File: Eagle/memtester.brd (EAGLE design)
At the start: 80.1 x 23.2 mm, 4 parts

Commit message: Memtester: part work backup
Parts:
- added U$2, U$3: PCF8575TS, PCF8575TS:SSOP24
- U$1: value NN5118160AJ -> NN5118160AJSOCKET; device AtariST:SOJ127P1117X376-42 -> memory:SOJ42SOCKET
- moved C3 28.4 mm to (9.91, 1.46), flipped to the bottom
- moved C2 11.4 mm to (33.1, 5.96), flipped to the bottom
- moved C1 11.4 mm to (1.99, 5.90), flipped to the bottom
- moved U$1 6.85 mm to (17.5, 12.1), turned to 0 degrees
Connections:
- new net A0: U$1.17, U$3.4
- new net A1: U$1.18, U$3.5
- new net A2: U$1.19, U$3.6
- new net A3: U$1.20, U$3.7
- new net A4: U$1.23, U$3.8
- new net A5: U$1.24, U$3.9
- new net A6: U$1.25, U$3.10
- new net A7: U$1.26, U$3.11
- new net A8: U$1.27, U$3.13
- new net A9: U$1.28, U$3.14
- new net D0: U$1.2, U$2.4
- new net D1: U$1.3, U$2.5
- new net D10: U$1.35, U$2.15
- new net D11: U$1.36, U$2.16
- new net D12: U$1.38, U$2.17
- new net D13: U$1.39, U$2.18
- new net D14: U$1.40, U$2.19
- new net D15: U$1.41, U$2.20
- new net D2: U$1.4, U$2.6
- new net D3: U$1.5, U$2.7
- new net D4: U$1.7, U$2.8
- new net D5: U$1.8, U$2.9
- new net D6: U$1.9, U$2.10
- new net D7: U$1.10, U$2.11
- new net D8: U$1.33, U$2.13
- new net D9: U$1.34, U$2.14
- new net I2C_SCL: U$2.22, U$3.22
- new net I2C_SDA: U$2.23, U$3.23
- net +5V: now also U$2.21, U$2.24, U$2.3, U$3.24, U$3.3
- net GND: now also U$2.12, U$2.2, U$3.12, U$3.2, U$3.21
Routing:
- net D0: track 0.00 -> 43.7 mm
- net D14: track 0.00 -> 39.7 mm
- net D2: track 0.00 -> 39.7 mm
- net D15: track 0.00 -> 39.2 mm
- net D1: track 0.00 -> 39.0 mm
- net A0: track 0.00 -> 37.8 mm
- net A9: track 0.00 -> 37.0 mm, vias 0 -> 1
- net D12: track 0.00 -> 36.1 mm
- net D13: track 0.00 -> 35.4 mm
- net D3: track 0.00 -> 35.3 mm
- net A7: track 0.00 -> 35.0 mm, vias 0 -> 1
- net A2: track 0.00 -> 34.0 mm
- net A5: track 0.00 -> 33.8 mm, vias 0 -> 1
- net A1: track 0.00 -> 33.5 mm
- net D11: track 0.00 -> 32.9 mm
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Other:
- board size 80.1 x 23.2 mm -> 69 x 22.6 mm
- board text added: "MEMTester"
- board text removed: "STRam Rev.C"

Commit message: Memtester: part work
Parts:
- added C4: 100nF, resistor:C0402
- added C5, C6: 100nF, passives:0402_CAP
- added IC1: HT7833, holtek2:SOT-89
- added J3: SM08B-SRSS-TB(LF)(SN), SM08B-SRSS-TB_LF__SN_:JST_SM08B-SRSS-TB(LF)(SN)
- added PROG: (no value), pinhead:1X03
- added U$6: OLED_0.96_I2CNO_DRILL, tft_1_8_1_44_oled_0_96:OLED_0.96_I2C_NO_DRILL
- added U1: ATTINY1616-MFR, ATTINY1616-MFR:QFN40P300X300X90-21N
- added UART: (no value), pinhead:1X04
- C1, C2, C3: device rcl:C0805 -> passives:0402_CAP
- moved U$3 2.25 mm to (49.8, 12.1)
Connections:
- new net EXTCLK: U1.2
- new net N$1: IC1.1, U$6.VCC
- new net OE: U$1.29, U$3.17
- new net PA5: U1.6
- new net PA6: U1.7
- new net PA7: U1.8
- new net PB2: U1.12
- new net PB3: U1.11
- new net PB4: U1.10
- new net PB5: U1.9
- new net RTS: U1.5
- new net RXD: U1.1, UART.2
- new net SPI_CS: J3.5, U1.18
- new net SPI_MISO: J3.6, U1.16
- new net SPI_MOSI: J3.3, U1.17
- new net SPI_SCLK: J3.4, U1.15
- new net TINY_RST: PROG.1, U1.19
- new net TXD: U1.20, UART.1
- net +5V: now also C4.1, C5.1, C6.1, IC1.3, IC1.4, J3.2, PROG.2, U1.4, UART.3
- net CAS0H: now also U$3.16
- net CAS0L: now also U$3.15
- net GND: now also C4.2, C5.2, C6.2, IC1.2, J3.1, PROG.3, U$6.GND, U1.21, U1.3, UART.4; no longer U$1.29
- net I2C_SCL: now also J3.7, U$6.SCL, U1.14
- net I2C_SDA: now also J3.8, U$6.SDA, U1.13
- net WE: now also U$3.18
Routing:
- net +5V: track 10.2 -> 147.9 mm, vias 0 -> 6
- net WE: track 0.00 -> 39.0 mm, vias 0 -> 1
- net CAS0L: track 0.00 -> 37.1 mm, vias 0 -> 1
- net I2C_SCL: track 0.00 -> 36.4 mm, vias 0 -> 2
- net OE: track 0.00 -> 35.2 mm, vias 0 -> 1
- net I2C_SDA: track 0.00 -> 33.4 mm, vias 0 -> 2
- net CAS0H: track 0.00 -> 33.1 mm, vias 0 -> 1
- net N$1: track 0.00 -> 14.3 mm
- net SPI_CS: track 0.00 -> 13.1 mm, vias 0 -> 2
- net TINY_RST: track 0.00 -> 12.8 mm
- net SPI_MOSI: track 0.00 -> 12.7 mm, vias 0 -> 2
- net SPI_MISO: track 0.00 -> 11.4 mm, vias 0 -> 2
- net SPI_SCLK: track 0.00 -> 10.8 mm, vias 0 -> 2
- net TXD: track 0.00 -> 9.25 mm, vias 0 -> 1
- net RXD: track 0.00 -> 8.25 mm, vias 0 -> 1
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- added copper zone on layer 1, net GND
- removed copper zone on layer 1, net +5V
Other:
- board size 69 x 22.6 mm -> 69 x 22.3 mm
- board text added: "5V"
- board text added: "CS"
- board text added: "GND"
- board text added: "MISO"
- board text added: "MOSI"
- board text added: "RST"
- board text added: "RX0"
- board text added: "SCL"
- board text added: "SCLK"
- board text added: "SDA"
- board text added: "TX0"

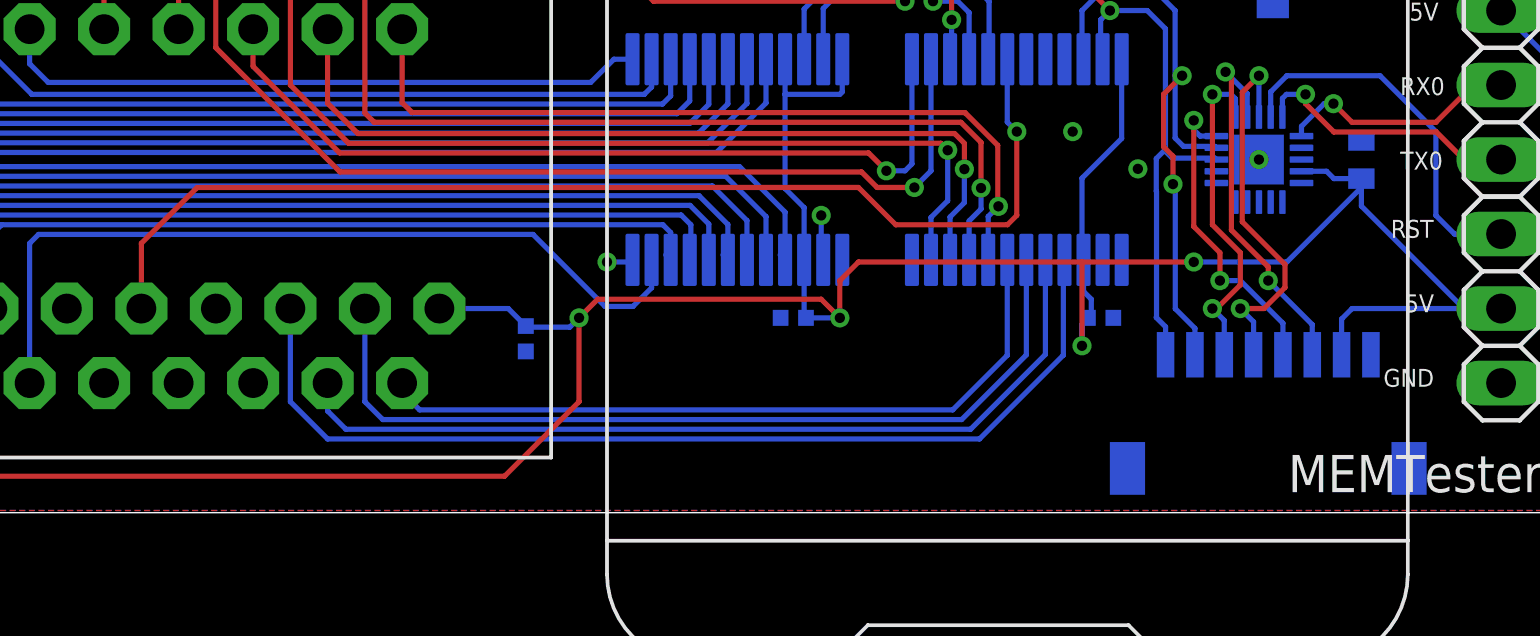
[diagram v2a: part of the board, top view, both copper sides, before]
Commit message: Memtester: routed RAS0
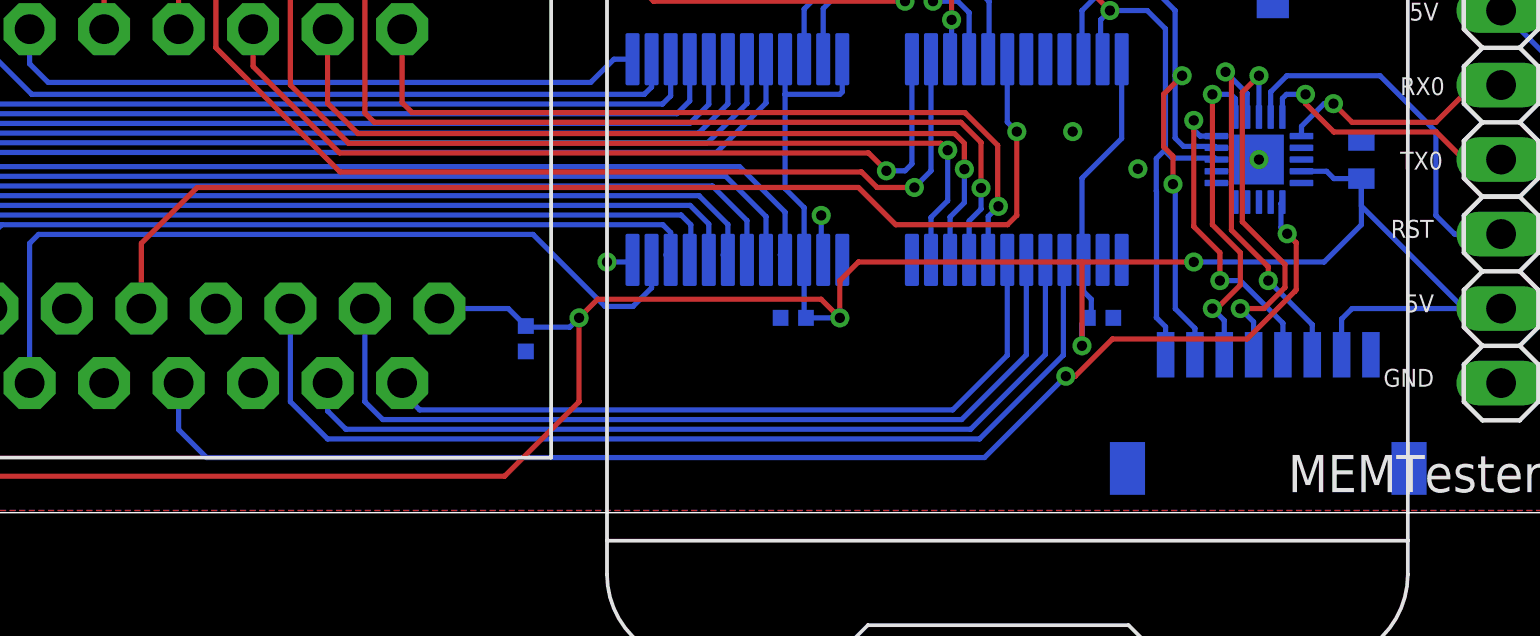
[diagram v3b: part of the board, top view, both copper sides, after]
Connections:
- removed net PA5: U1.6
- net RAS0: now also U1.6
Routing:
- net RAS0: track 0.00 -> 45.7 mm, vias 0 -> 2
- net +5V: track 147.9 -> 148.6 mm
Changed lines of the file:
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@@
 <wire x1="52.07" y1="6.46556875" x2="52.07" y2="5.715" width="0.1778" layer="16"/>
 <via x="52.07" y="5.715" extent="1-16" drill="0.35"/>
-<wire x1="61.595" y1="11.415" x2="61.595" y2="11.1125" width="0.1778" layer="16"/>
-<wire x1="61.595" y1="11.1125" x2="59.055" y2="8.5725" width="0.1778" layer="16"/>
-<wire x1="59.055" y1="8.5725" x2="55.88" y2="8.5725" width="0.1778" layer="16"/>
+<wire x1="61.595" y1="11.415" x2="61.595" y2="9.8425" width="0.1778" layer="16"/>
+<wire x1="61.595" y1="9.8425" x2="60.325" y2="8.5725" width="0.1778" layer="16"/>
+<wire x1="60.325" y1="8.5725" x2="55.88" y2="8.5725" width="0.1778" layer="16"/>
 <contactref element="UART" pad="3"/>
 <wire x1="61.92750625" y1="11.415" x2="61.595" y2="11.415" width="0.1778" layer="16"/>
@@
 <signal name="RAS0">
 <contactref element="U$1" pad="14"/>
+<contactref element="U1" pad="6"/>
+<wire x1="22.225" y1="1.905" x2="21.2725" y2="2.8575" width="0.1778" layer="16"/>
+<wire x1="21.2725" y1="4.445" x2="21.2725" y2="2.8575" width="0.1778" layer="16"/>
+<wire x1="48.74676875" y1="1.905" x2="51.519634375" y2="4.677865625" width="0.1778" layer="16"/>
+<via x="51.519634375" y="4.677865625" extent="1-16" drill="0.35"/>
+<wire x1="59.3189" y1="7.56515625" x2="59.3189" y2="7.5664" width="0.1778" layer="1"/>
+<wire x1="59.3189" y1="7.5664" x2="59.3725" y2="7.62" width="0.1778" layer="1"/>
+<wire x1="53.107134375" y1="5.947865625" x2="51.837134375" y2="4.677865625" width="0.1778" layer="1"/>
+<wire x1="51.519634375" y1="4.677865625" x2="51.837134375" y2="4.677865625" width="0.1778" layer="1"/>
+<wire x1="57.701609375" y1="5.947865625" x2="53.107134375" y2="5.947865625" width="0.1778" layer="1"/>
+<wire x1="57.701609375" y1="5.947865625" x2="59.3189" y2="7.56515625" width="0.1778" layer="1"/>
+<wire x1="59.3725" y1="7.62" x2="59.3725" y2="9.2285375" width="0.1778" layer="1"/>
+<wire x1="59.3725" y1="9.2285375" x2="59.06551875" y2="9.53551875" width="0.1778" layer="1"/>
+<via x="59.06551875" y="9.53551875" extent="1-16" drill="0.35"/>
+<wire x1="59.06551875" y1="9.53551875" x2="58.8538" y2="9.7472375" width="0.1778" layer="16"/>
+<wire x1="58.8538" y1="10.5663" x2="58.8538" y2="9.7472375" width="0.1778" layer="16"/>
+<wire x1="58.8538" y1="10.5663" x2="58.9025" y2="10.615" width="0.1778" layer="16"/>
+<wire x1="22.225" y1="1.905" x2="48.74676875" y2="1.905" width="0.1778" layer="16"/>
 </signal>
 <signal name="CAS0H">
@@
 <contactref element="U1" pad="2"/>
 </signal>
-<signal name="PA5">
-<contactref element="U1" pad="6"/>
-</signal>
 <signal name="PA6">

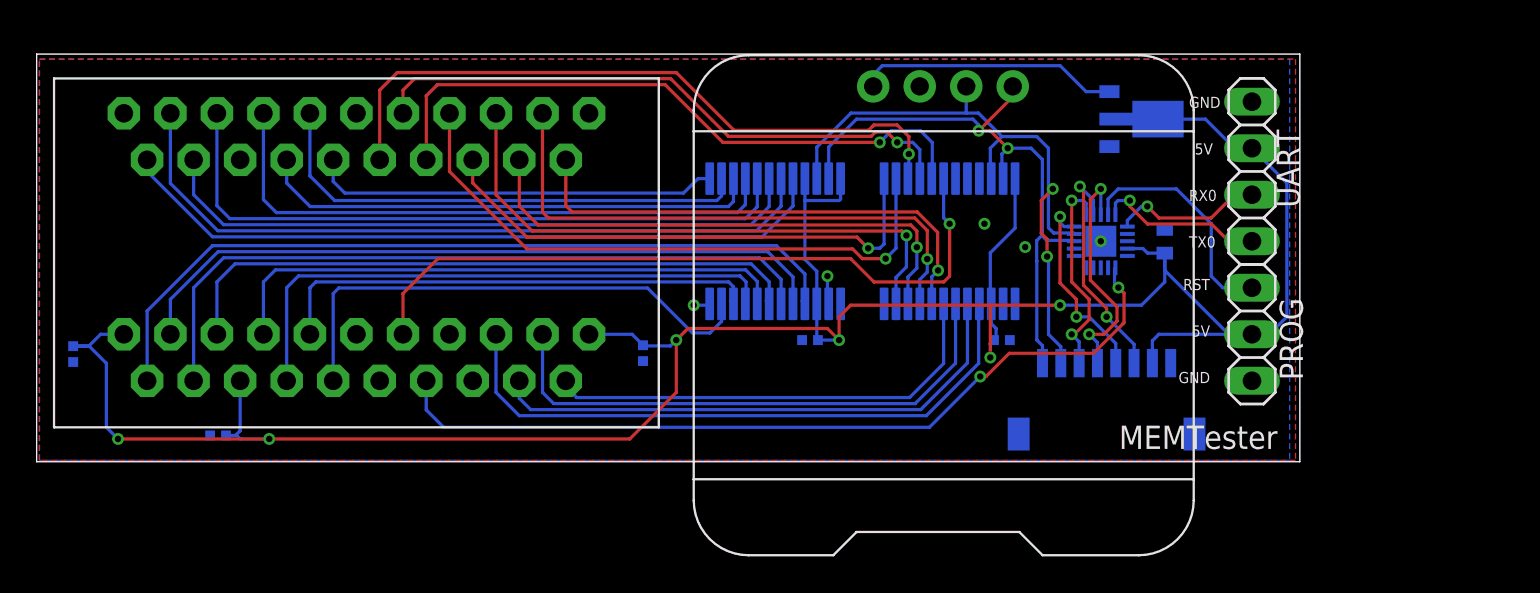
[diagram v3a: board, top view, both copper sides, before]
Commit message: Memtester: bigger 5v wire
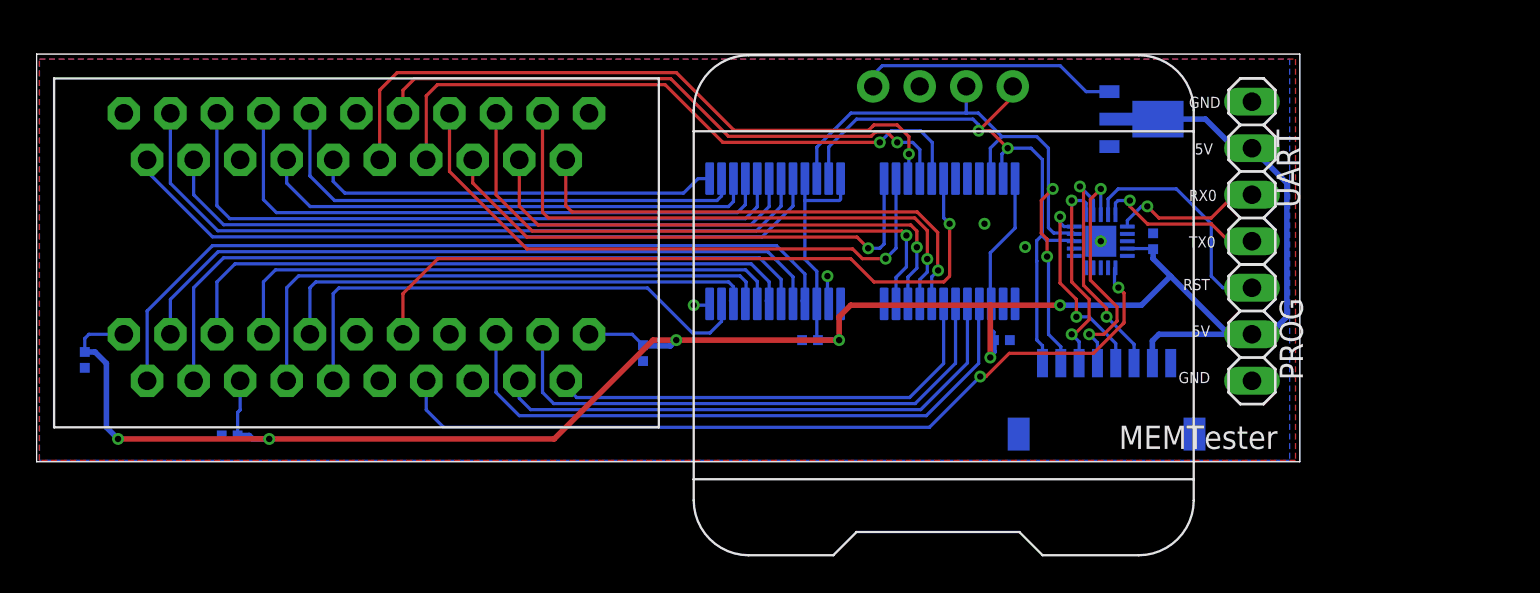
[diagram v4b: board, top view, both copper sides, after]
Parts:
- C4: device resistor:C0402 -> passives:0402_CAP
- moved C1 0.71 mm to (2.63, 5.59)
- moved C3 0.63 mm to (10.5, 1.46)
- moved C4 0.63 mm to (61.0, 12.1)
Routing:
- net +5V: track 148.6 -> 143.0 mm
